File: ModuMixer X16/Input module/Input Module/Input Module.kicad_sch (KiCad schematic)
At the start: 0 parts

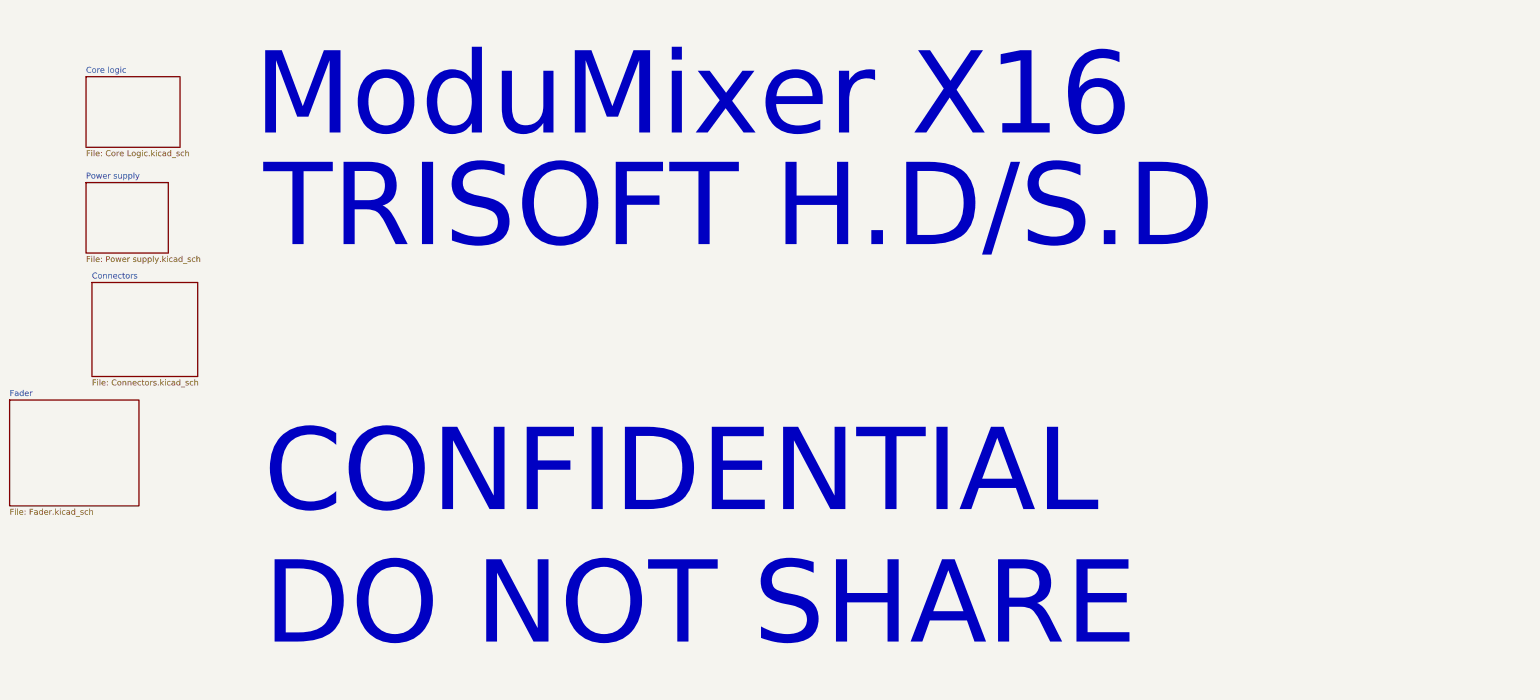
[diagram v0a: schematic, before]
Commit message: Added schematics pdf
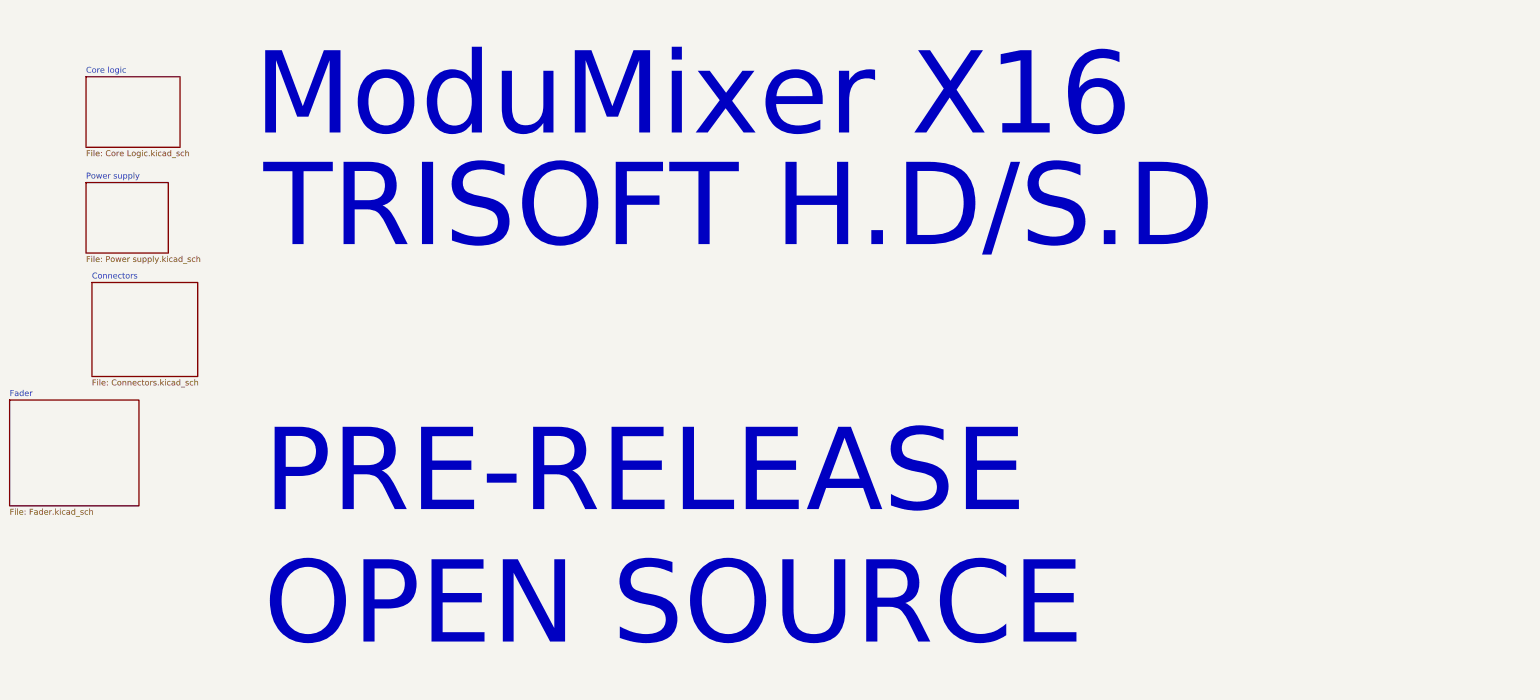
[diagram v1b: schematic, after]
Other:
- note added: "TRISOFT H.D/S.D PRE-RELEASE OPEN SOURCE"
- note removed: "TRISOFT H.D/S.D CONFIDENTIAL DO NOT SHARE"
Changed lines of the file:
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@@
 	(generator_version "8.0")
 	(paper "A4")
-	(text "TRISOFT H.D/S.D\n\nCONFIDENTIAL\nDO NOT SHARE"
+	(text "TRISOFT H.D/S.D\n\nPRE-RELEASE\nOPEN SOURCE"
 		(exclude_from_sim no)
 		(at 11.684 90.17 0)
